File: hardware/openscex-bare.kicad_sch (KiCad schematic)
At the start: 8 parts, among them U1 ATtiny85-20PU

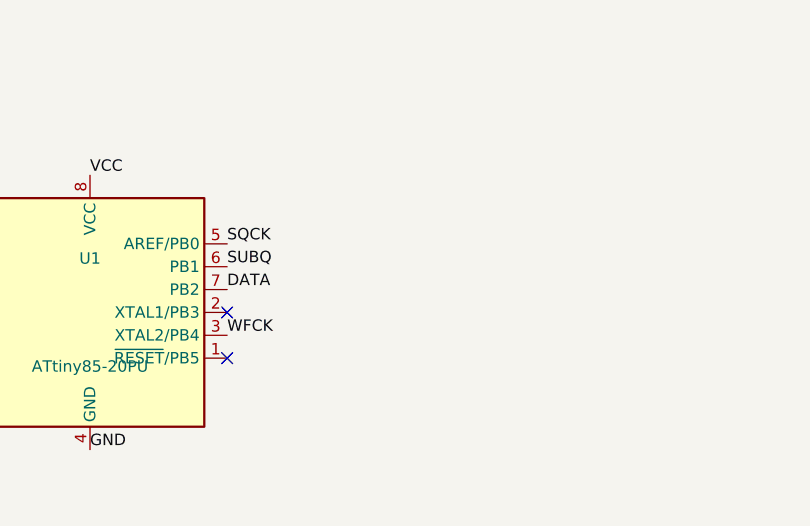
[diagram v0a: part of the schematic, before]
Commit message: feat(hardware): add a RESET pull-up to every board
The mini and bare boards now hold pin 1 high with a 10 kOhm pull-up,
as the carrier already did. The chip's own pull-up is 30 to 60 kOhm,
weak against noise coupled in from the console, and a spurious reset
costs the region check of the disc being read. Any ISP programmer
still overrides it.
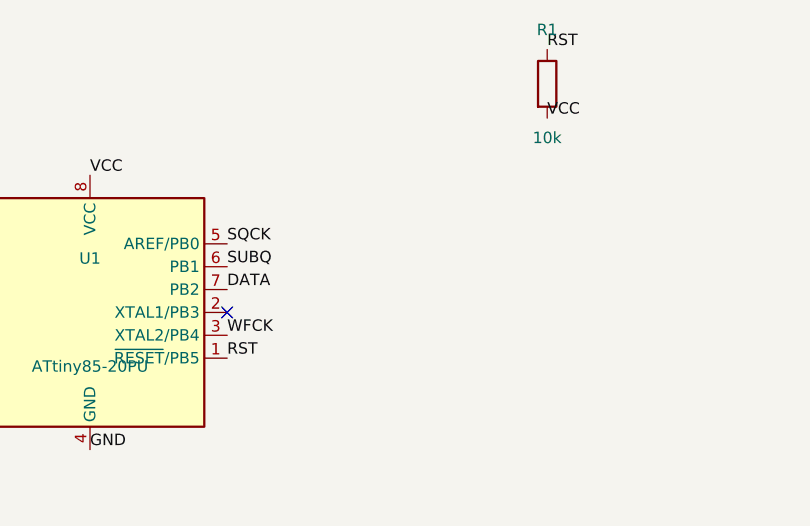
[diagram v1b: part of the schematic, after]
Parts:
- added R1: 10k, Resistor_THT:R_Axial_DIN0204_L3.6mm_D1.6mm_P5.08mm_Horizontal, symbol Device:R
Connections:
- net VCC: now also R1.2
- net RST: now reaches U1.1 (~{RESET}/PB5)
- net RST: now also R1.1
- no-connect marks 2 -> 1
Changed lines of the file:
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@@
 (kicad_sch (version 20231120) (generator "eeschema") (generator_version "8.0")
 	(paper "A3")
-	(title_block (title "openscex bare") (comment 1 "ATtiny85 PS1 modchip bare carrier: socket and decoupling"))
+	(title_block (title "openscex bare") (comment 1 "ATtiny85 PS1 modchip bare carrier: socket, decoupling, RESET pull-up"))
 (symbol (lib_id "MCU_Microchip_ATtiny:ATtiny85-20P") (at 76.2 76.2 0) (unit 1)
 	(in_bom yes) (on_board yes) (dnp no)
@@
 	(instances (project "openscex-bare" (path "/7206801e-1c20-5311-8a84-3899543930cc" (reference "U1") (unit 1))))
 )
-(no_connect (at 91.44 81.28))
+(label "RST" (at 91.44 81.28 0) (effects (font (size 1.27 1.27)) (justify left bottom)))
 (no_connect (at 91.44 76.2))
 (label "WFCK" (at 91.44 78.74 0) (effects (font (size 1.27 1.27)) (justify left bottom)))
@@
 (label "VCC" (at 38.1 72.39 0) (effects (font (size 1.27 1.27)) (justify left bottom)))
 (label "GND" (at 38.1 80.01 0) (effects (font (size 1.27 1.27)) (justify left bottom)))
+(symbol (lib_id "Device:R") (at 127.0 50.8 0) (unit 1)
+	(in_bom yes) (on_board yes) (dnp no)
+	(property "Reference" "R1" (at 127.0 44.8 0) (effects (font (size 1.27 1.27))))
+	(property "Value" "10k" (at 127.0 56.8 0) (effects (font (size 1.27 1.27))))
+	(property "Footprint" "Resistor_THT:R_Axial_DIN0204_L3.6mm_D1.6mm_P5.08mm_Horizontal" (at 127.0 50.8 0) (effects (font (size 1.27 1.27)) (hide yes)))
+	(property "Datasheet" "" (at 127.0 50.8 0) (effects (font (size 1.27 1.27)) (hide yes)))
+	(property "Part" "10 kOhm axial resistor, DIN0204, 5.08 mm pitch" (at 127.0 50.8 0) (effects (font (size 1.27 1.27)) (hide yes)))
+	(pin "1")
+	(pin "2")
+	(instances (project "openscex-bare" (path "/7206801e-1c20-5311-8a84-3899543930cc" (reference "R1") (unit 1))))
+)
+(label "RST" (at 127.0 46.99 0) (effects (font (size 1.27 1.27)) (justify left bottom)))
+(label "VCC" (at 127.0 54.61 0) (effects (font (size 1.27 1.27)) (justify left bottom)))
 (symbol (lib_id "Connector:TestPoint") (at 50.8 139.7 0) (unit 1)
 	(in_bom no) (on_board yes) (dnp no)

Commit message: feat(hardware): name datasheet-checked parts
Every BOM line now names an exact manufacturer part, each checked
against its own datasheet: Microchip ATTINY85-20PU in a TE
1-2199298-2 socket, KEMET C315C104K5R5TA, Panasonic EEU-FC1A101S,
Vishay MBA0204 resistors, onsemi 2N3904RLRAG and 1N4148TR,
Kingbright WP710A10ID, CTS 206-2ST, Same Sky CMI-1295IC-0385T and
Wurth 61200621621.

C1 moves to a 4.0 x 2.5 mm footprint that fits the KEMET body. A
project footprint library, hardware/openscex.pretty, carries the hole
sizes the Wurth header and the buzzer datasheets recommend, 1.1 mm and
0.8 mm in 2 mm pads.
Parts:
- C1: footprint Capacitor_THT:C_Disc_D3.0mm_W1.6mm_P2.50mm -> Capacitor_THT:C_Rect_L4.0mm_W2.5mm_P2.50mm; Part 100 nF ceramic disc, 50 V, 2.5 mm pitch -> KEMET C315C104K5R5TA, 100 nF 50 V X7R, 2.54 mm
- R1: Part 10 kOhm axial resistor, DIN0204, 5.08 mm pitch -> Vishay MBA02040C1002FC100, 10 kOhm 1 % 0.4 W, 0204
- U1: Part ATtiny85-20PU in a DIP-8 7.62 mm socket -> Microchip ATTINY85-20PU in a TE 1-2199298-2 DIP-8 socket
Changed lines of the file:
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@@
 	(property "Footprint" "Package_DIP:DIP-8_W7.62mm_Socket" (at 76.2 76.2 0) (effects (font (size 1.27 1.27)) (hide yes)))
 	(property "Datasheet" "" (at 76.2 76.2 0) (effects (font (size 1.27 1.27)) (hide yes)))
-	(property "Part" "ATtiny85-20PU in a DIP-8 7.62 mm socket" (at 76.2 76.2 0) (effects (font (size 1.27 1.27)) (hide yes)))
+	(property "Part" "Microchip ATTINY85-20PU in a TE 1-2199298-2 DIP-8 socket" (at 76.2 76.2 0) (effects (font (size 1.27 1.27)) (hide yes)))
 	(pin "1")
 	(pin "2")
@@
 	(property "Reference" "C1" (at 38.1 70.2 0) (effects (font (size 1.27 1.27))))
 	(property "Value" "100nF" (at 38.1 82.2 0) (effects (font (size 1.27 1.27))))
-	(property "Footprint" "Capacitor_THT:C_Disc_D3.0mm_W1.6mm_P2.50mm" (at 38.1 76.2 0) (effects (font (size 1.27 1.27)) (hide yes)))
+	(property "Footprint" "Capacitor_THT:C_Rect_L4.0mm_W2.5mm_P2.50mm" (at 38.1 76.2 0) (effects (font (size 1.27 1.27)) (hide yes)))
 	(property "Datasheet" "" (at 38.1 76.2 0) (effects (font (size 1.27 1.27)) (hide yes)))
-	(property "Part" "100 nF ceramic disc, 50 V, 2.5 mm pitch" (at 38.1 76.2 0) (effects (font (size 1.27 1.27)) (hide yes)))
+	(property "Part" "KEMET C315C104K5R5TA, 100 nF 50 V X7R, 2.54 mm" (at 38.1 76.2 0) (effects (font (size 1.27 1.27)) (hide yes)))
 	(pin "1")
 	(pin "2")
@@
 	(property "Footprint" "Resistor_THT:R_Axial_DIN0204_L3.6mm_D1.6mm_P5.08mm_Horizontal" (at 127.0 50.8 0) (effects (font (size 1.27 1.27)) (hide yes)))
 	(property "Datasheet" "" (at 127.0 50.8 0) (effects (font (size 1.27 1.27)) (hide yes)))
-	(property "Part" "10 kOhm axial resistor, DIN0204, 5.08 mm pitch" (at 127.0 50.8 0) (effects (font (size 1.27 1.27)) (hide yes)))
+	(property "Part" "Vishay MBA02040C1002FC100, 10 kOhm 1 % 0.4 W, 0204" (at 127.0 50.8 0) (effects (font (size 1.27 1.27)) (hide yes)))
 	(pin "1")
 	(pin "2")
